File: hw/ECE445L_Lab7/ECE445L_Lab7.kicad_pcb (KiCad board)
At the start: 2 copper layers, 152.4 x 127 mm, 214 parts, among them J1 2479774-1, J2 EK-TM4C123GXL, J4 AudioJack, Q1 MMBF170, Q10 MMBF170, Q11 MMBF170, Q12 MMBF170, Q13 MMBF170, Q14 MMBF170, Q15 MMBF170, Q16 MMBF170, Q17 MMBF170, Q18 MMBF170, Q2 MMBF170, Q3 MMBF170, Q4 MMBF170, Q5 MMBF170, Q6 MMBF170, Q7 MMBF170, Q8 MMBF170, Q9 MMBF170, SW1 SW_SPST, SW2 Pause, SW3 LCDMode, SW4 Flanger, SW5 Distortion, SW6 Reverb, SW7 Delay, SW8 Tempo, U1 LM2937ET-3.3_NOPB, U10 TLV5616, U11 OPA2350, U12 OPA2350, U13 OPA2350, U14 OPA2350, U15 TLV5616, U16 Adafruit ST7735R, U2 LM4041CILPR, U3 ESP32-D0WD-V3, U5 FT232R, U6 OPA2350, U7 OPA2350, U8 OPA2350, U9 OPA2350

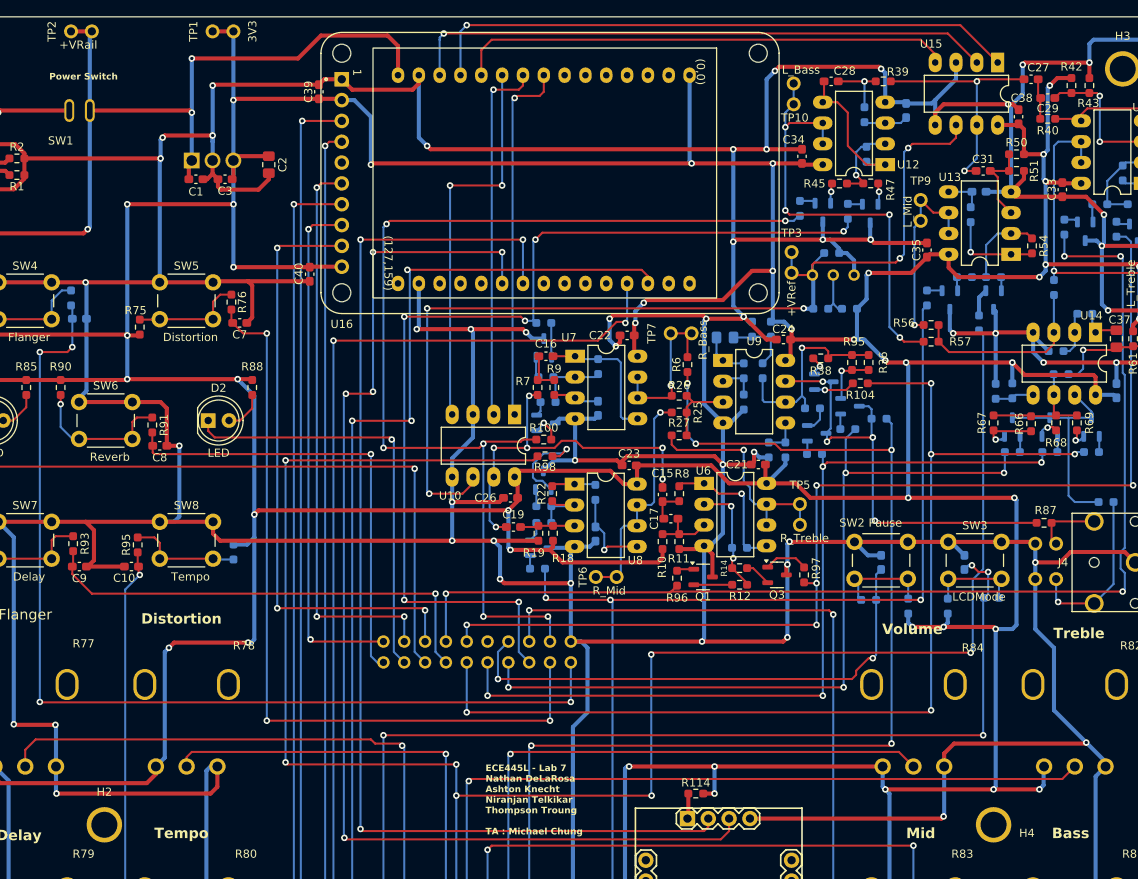
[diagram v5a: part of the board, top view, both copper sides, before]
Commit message: Hardware layout - fixed voltage reference
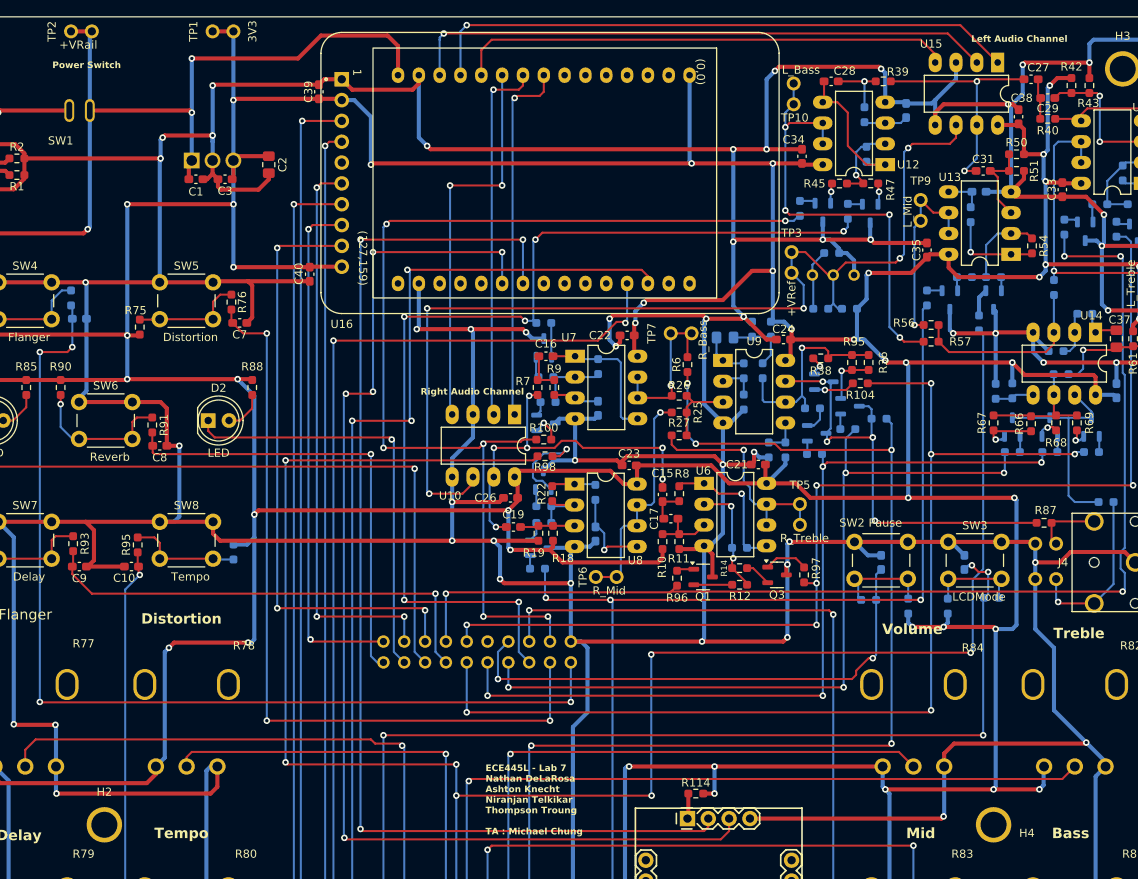
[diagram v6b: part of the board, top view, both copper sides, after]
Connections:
- R3 pad 2: Net-(R3-Pad2) -> VRef
- R4 pad 1: Net-(R3-Pad2) -> VRef
- R4 pad 2: VRef -> Net-(R4-Pad2)
- R5 pad 1: VRef -> Net-(R4-Pad2)
- U2 pad 1: VRef -> Net-(R4-Pad2)
- U2 pad 2: Net-(R3-Pad2) -> VRef
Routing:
- net Net-(R4-Pad2): track 0.00 -> 7.44 mm
- net Net-(R3-Pad2): track 5.69 -> 0.00 mm
- net VRef: track 122.0 -> 124.7 mm
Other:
- board text added: "Left Audio Channel"
- board text added: "Right Audio Channel"
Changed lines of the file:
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@@
 	(net 133 "Net-(C28-Pad2)")
 	(net 134 "Net-(C37-Pad2)")
-	(net 135 "Net-(R3-Pad2)")
+	(net 135 "Net-(R4-Pad2)")
 	(net 136 "Net-(Q7-B)")
 	(net 137 "unconnected-(U3-GPIO33-Pad7)")
@@
 		(at 101.6 44.45 -90)
 		(property "Reference" "U16"
-			(at 18.4404 25.4 180)
+			(at 18.4404 25.4 0)
 			(layer "F.SilkS")
 			(effects
@@
 		)
 		(fp_text user "(127,159)"
-			(at 7.62 20.32 270)
+			(at 7.0104 23.4188 270)
 			(unlocked yes)
 			(layer "F.SilkS")
@@
 			)
 		)
-		(pad "" np_thru_hole circle
-			(at -14.605 -25.4)
-			(size 2.2 2.2)
-			(drill 2.2)
-			(layers "*.Cu" "*.Mask")
-		)
-		(pad "" np_thru_hole circle
-			(at -14.605 25.4)
-			(size 2.2 2.2)
-			(drill 2.2)
-			(layers "*.Cu" "*.Mask")
-		)
-		(pad "" np_thru_hole circle
-			(at 14.605 -25.4)
-			(size 2.2 2.2)
-			(drill 2.2)
-			(layers "*.Cu" "*.Mask")
-		)
-		(pad "" np_thru_hole circle
-			(at 14.605 25.4)
-			(size 2.2 2.2)
-			(drill 2.2)
-			(layers "*.Cu" "*.Mask")
-		)
 		(pad "1" thru_hole rect
 			(at -11.43 25.4)
@@
 		)
 		(fp_line
-			(start -14.611 6.532)
-			(end -13.976 5.897)
-			(stroke
-				(width 0.2032)
-				(type solid)
-			)
-			(layer "F.SilkS")
-		)
-		(fp_line
-			(start -16.516 5.897)
-			(end -15.881 6.532)
-			(stroke
-				(width 0.2032)
-				(type solid)
-			)
-			(layer "F.SilkS")
-		)
-		(fp_line
 			(start -16.516 5.897)
 			(end -16.516 4.627)
@@
 		)
 		(fp_line
-			(start -16.516 4.627)
-			(end -15.881 3.992)
-			(stroke
-				(width 0.2032)
-				(type solid)
-			)
-			(layer "F.SilkS")
-		)
-		(fp_line
 			(start -13.976 4.627)
 			(end -13.976 5.897)
@@
 		)
 		(fp_line
-			(start -14.611 3.992)
-			(end -13.976 4.627)
-			(stroke
-				(width 0.2032)
-				(type solid)
-			)
-			(layer "F.SilkS")
-		)
-		(fp_line
 			(start -16.516 3.357)
 			(end -16.516 2.087)
@@
 			(layers "B.Cu" "B.Mask" "B.Paste")
 			(roundrect_rratio 0.25)
-			(net 135 "Net-(R3-Pad2)")
+			(net 100 "VRef")
 			(pintype "passive")
 		)
@@
 		)
 		(group ""
-			(members "11c5cd52-69f3-4446-bccb-5f9518d66313" "30eab901-faa1-48e6-9f11-a2470f24fe87"
-				"370ae8a8-94fd-461e-bf20-ddbf13826b6e" "3973a864-3621-4e61-8c96-8c65e393ac25"
-				"49d39620-b9be-450e-880b-1048b977e30c" "5eb9c70e-c6af-42c4-9062-bd827725a32c"
-				"678d534d-a7ca-4aa0-9f1e-a9d111543dec" "7488b676-18a6-4ed4-92f7-680afbb5b136"
-				"8022baee-523a-44e4-9ba1-32b8b3af9ea7" "9fb0d361-2e3e-429f-9451-9d610e9aa400"
-				"b61cd692-3c2b-4db4-a00d-1b86db24f691" "be1a233e-ac1f-4e60-93fe-5c93686e9edc"
-				"dd1363e2-d05e-4584-94b3-d17287d31c97" "ddfc8a73-91ee-4b8f-9319-b5ca49929a30"
-				"ee488e86-51e9-44a6-80ee-4de8811c40bf"
-			)
-		)
-		(group ""
 			(members "05085929-df47-4023-ada3-8e05809de806" "0d1c2b11-0e75-4697-914f-baecb480edc5"
 				"0d325539-8a40-476c-8c19-a88dd3c161f2" "1d2eddcb-aa38-4ea7-9334-7ec7fefdf58d"
@@
 			)
 		)
+		(group ""
+			(members "11c5cd52-69f3-4446-bccb-5f9518d66313" "30eab901-faa1-48e6-9f11-a2470f24fe87"
+				"370ae8a8-94fd-461e-bf20-ddbf13826b6e" "3973a864-3621-4e61-8c96-8c65e393ac25"
+				"49d39620-b9be-450e-880b-1048b977e30c" "5eb9c70e-c6af-42c4-9062-bd827725a32c"
+				"678d534d-a7ca-4aa0-9f1e-a9d111543dec" "7488b676-18a6-4ed4-92f7-680afbb5b136"
+				"8022baee-523a-44e4-9ba1-32b8b3af9ea7" "9fb0d361-2e3e-429f-9451-9d610e9aa400"
+				"b61cd692-3c2b-4db4-a00d-1b86db24f691" "be1a233e-ac1f-4e60-93fe-5c93686e9edc"
+				"dd1363e2-d05e-4584-94b3-d17287d31c97" "ddfc8a73-91ee-4b8f-9319-b5ca49929a30"
+				"ee488e86-51e9-44a6-80ee-4de8811c40bf"
+			)
+		)
 		(embedded_fonts no)
 		(model "${KICAD_USER_3DMODELS}/ESP32-30pin.step"
@@
 		(tags "SOT TO_SOT_SMD")
 		(property "Reference" "Q12"
-			(at 0 -2.4892 -90)
+			(at 0 -2.4892 270)
 			(layer "B.SilkS")
 			(effects
@@
 		(sheetname "/Lab7_microcontroller/")
 		(sheetfile "Lab7_microcontroller.kicad_sch")
-		(attr through_hole)
+		(attr through_hole allow_missing_courtyard)
 		(fp_line
 			(start 25.4 -33.02)
@@
 			(layers "B.Cu" "B.Mask" "B.Paste")
 			(roundrect_rratio 0.25)
-			(net 135 "Net-(R3-Pad2)")
+			(net 100 "VRef")
 			(pintype "passive")
 		)
@@
 			(layers "B.Cu" "B.Mask" "B.Paste")
 			(roundrect_rratio 0.25)
-			(net 100 "VRef")
+			(net 135 "Net-(R4-Pad2)")
 			(pintype "passive")
 		)
@@
 			(layers "B.Cu" "B.Mask" "B.Paste")
 			(roundrect_rratio 0.25)
-			(net 100 "VRef")
+			(net 135 "Net-(R4-Pad2)")
 			(pintype "passive")
 		)
@@
 			(layers "*.Cu" "*.Mask")
 			(remove_unused_layers no)
-			(net 100 "VRef")
+			(net 135 "Net-(R4-Pad2)")
 			(pintype "passive")
 			(solder_mask_margin 0.102)
@@
 			(layers "*.Cu" "*.Mask")
 			(remove_unused_layers no)
-			(net 135 "Net-(R3-Pad2)")
+			(net 100 "VRef")
 			(pintype "passive")
 			(solder_mask_margin 0.102)
@@
 		)
 	)
+	(gr_text "Right Audio Channel"
+		(at 85.8012 71.5772 0)
+		(layer "F.SilkS")
+		(effects
+			(font
+				(size 0.8 0.8)
+				(thickness 0.15)
+				(bold yes)
+			)
+			(justify left bottom)
+		)
+	)
 	(gr_text "Flanger"
 		(at 37.592 99.06 0)
@@
 		)
 	)
+	(gr_text "Left Audio Channel"
+		(at 152.9588 28.5496 0)
+		(layer "F.SilkS")
+		(effects
+			(font
+				(size 0.8 0.8)
+				(thickness 0.15)
+				(bold yes)
+			)
+			(justify left bottom)
+		)
+	)
 	(gr_text "Volume"
 		(at 145.796 100.838 0)
@@
 	)
 	(gr_text "Power Switch"
-		(at 40.513 33.147 0)
+		(at 40.894 31.75 0)
 		(layer "F.SilkS")
 		(effects
@@
 	)
 	(segment
-		(start 133.858 55.372)
-		(end 133.604 55.626)
+		(start 136.144 56.896)
+		(end 135.5344 56.896)
 		(width 0.25)
 		(layer "F.Cu")
@@
 	)
 	(segment
+		(start 136.144 56.896)
+		(end 137.668 55.372)
+		(width 0.25)
+		(layer "F.Cu")
+		(net 100)
+	)
+	(segment
+		(start 135.5344 56.896)
+		(end 132.7354 54.097)
+		(width 0.25)
+		(layer "F.Cu")
+		(net 100)
+	)
+	(segment
 		(start 86.868 83.566)
 		(end 90.932 83.566)
@@
 	)
 	(segment
-		(start 133.604 56.896)
-		(end 131.323 56.896)
+		(start 137.668 55.372)
+		(end 143.764 55.372)
 		(width 0.25)
 		(layer "F.Cu")
@@
 	)
 	(segment
-		(start 143.764 55.372)
-		(end 133.858 55.372)
+		(start 132.7354 54.097)
+		(end 131.064 54.097)
 		(width 0.25)
 		(layer "F.Cu")
@@
 	)
 	(segment
-		(start 133.604 55.626)
-		(end 133.604 56.896)
-		(width 0.25)
-		(layer "F.Cu")
-		(net 100)
-	)
-	(segment
 		(start 86.614 60.96)
 		(end 132.5372 60.96)
@@
 	)
 	(segment
+		(start 131.064 56.637)
+		(end 132.5372 58.1102)
+		(width 0.25)
+		(layer "B.Cu")
+		(net 100)
+	)
+	(segment
 		(start 144.272 54.864)
 		(end 144.78 54.356)
@@
 	)
 	(segment
-		(start 131.064 56.637)
-		(end 131.064 54.097)
+		(start 136.144 56.896)
+		(end 136.144 60.3993)
 		(width 0.25)
 		(layer "B.Cu")
@@
 	)
 	(segment
-		(start 133.7075 61.0108)
-		(end 132.588 61.0108)
-		(width 0.5)
+		(start 136.144 60.3993)
+		(end 135.5325 61.0108)
+		(width 0.25)
 		(layer "B.Cu")
 		(net 100)
 	)
 	(segment
-		(start 133.604 55.646403)
-		(end 135.0405 54.209903)
+		(start 131.064 56.637)
+		(end 131.064 54.097)
 		(width 0.25)
 		(layer "B.Cu")
@@
 	)
 	(segment
-		(start 133.604 56.896)
-		(end 133.604 55.646403)
+		(start 137.2127 61.0108)
+		(end 136.7555 61.0108)
 		(width 0.25)
 		(layer "B.Cu")
@@
 	)
 	(segment
-		(start 133.7075 56.9995)
-		(end 133.604 56.896)
-		(width 0.5)
+		(start 132.5372 58.1102)
+		(end 132.5372 60.96)
+		(width 0.25)
 		(layer "B.Cu")
 		(net 100)
 	)
 	(segment
-		(start 133.7075 61.0108)
-		(end 133.7075 56.9995)
-		(width 0.5)
+		(start 136.7555 61.0108)
+		(end 136.144 60.3993)
+		(width 0.25)
 		(layer "B.Cu")
 		(net 100)
@@
 	)
 	(segment
-		(start 136.144 56.896)
-		(end 136.144 60.3993)
+		(start 133.7075 61.0108)
+		(end 133.7075 56.9995)
 		(width 0.25)
 		(layer "B.Cu")
@@
 	)
 	(segment
-		(start 136.144 60.3993)
-		(end 135.5325 61.0108)
+		(start 133.604 55.646403)
+		(end 135.0405 54.209903)
 		(width 0.25)
 		(layer "B.Cu")
@@
 	)
 	(segment
-		(start 137.2127 61.0108)
-		(end 136.7555 61.0108)
+		(start 133.7075 56.9995)
+		(end 133.604 56.896)
 		(width 0.25)
 		(layer "B.Cu")
@@
 	)
 	(segment
-		(start 136.7555 61.0108)
-		(end 136.144 60.3993)
+		(start 133.604 56.896)
+		(end 133.604 55.646403)
 		(width 0.25)
 		(layer "B.Cu")

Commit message: Pushing so i can work on my desktop
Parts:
- added TP11: R_Out, ECE445L:Testpoint_1x02_P2.54mm, F.Cu at (175.2, 79.6)
- added TP12: L_Out, ECE445L:Testpoint_1x02_P2.54mm, F.Cu at (175.3, 71.8)
- moved C39 0.61 mm to (72.8, 34.6)
- moved U5 0.28 mm to (123.4, 138.2)
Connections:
- U3 pad 1: +3V3 -> +VRail
- U3 pad 10: RAUDIO_FS -> unconnected-(U3-GPIO32-Pad10)
- U3 pad 11: LAUDIO_FS -> unconnected-(U3-GPIO35-Pad11)
- U3 pad 12: LAUDIO_OUT -> unconnected-(U3-GPIO34-Pad12)
- U3 pad 13: LAUDIO_CLK -> unconnected-(U3-GPIO39-Pad13)
- U3 pad 14: GND -> unconnected-(U3-GPIO36-Pad14)
- U3 pad 15: +VRail -> +3V3
- U3 pad 17: unconnected-(U3-GPIO22-Pad17) -> GND
- U3 pad 18: PB0 -> unconnected-(U3-GPIO15-Pad18)
- U3 pad 19: PB1 -> unconnected-(U3-GPIO2-Pad19)
- U3 pad 2: unconnected-(U3-GPIO36-Pad2) -> GND
- U3 pad 21: unconnected-(U3-GPIO19-Pad21) -> ESP_OUT_USB_IN
- U3 pad 22: unconnected-(U3-GPIO18-Pad22) -> ESP_IN_USB_OUT
- U3 pad 24: ESP_IN_USB_OUT -> unconnected-(U3-GPIO18-Pad24)
- U3 pad 25: ESP_OUT_USB_IN -> unconnected-(U3-GPIO19-Pad25)
- U3 pad 27: unconnected-(U3-GPIO2-Pad27) -> PB1
- U3 pad 28: unconnected-(U3-GPIO15-Pad28) -> PB0
- U3 pad 29: GND -> unconnected-(U3-GPIO22-Pad29)
- U3 pad 3: unconnected-(U3-GPIO39-Pad3) -> LAUDIO_CLK
- U3 pad 4: unconnected-(U3-GPIO34-Pad4) -> LAUDIO_OUT
- U3 pad 5: unconnected-(U3-GPIO35-Pad5) -> LAUDIO_FS
- U3 pad 6: unconnected-(U3-GPIO32-Pad6) -> RAUDIO_FS
- U3 pad 7: unconnected-(U3-GPIO33-Pad7) -> RAUDIO_CLK
- U3 pad 9: RAUDIO_CLK -> unconnected-(U3-GPIO33-Pad9)
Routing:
- net GND: track 1171.8 -> 1129.7 mm, vias 54 -> 53
- net +VRail: track 271.3 -> 303.9 mm
- net PB0: track 150.1 -> 121.2 mm, vias 5 -> 4
- net LAUDIO_CLK: track 71.8 -> 46.2 mm
- net R_AudioOut: track 54.4 -> 77.1 mm, vias 4 -> 6
- net +3V3: track 910.0 -> 889.6 mm, vias 48 -> 45
- net LAUDIO_OUT: track 73.1 -> 52.9 mm
- net PB1: track 144.4 -> 125.3 mm
- net LAUDIO_FS: track 59.7 -> 44.7 mm, vias 0 -> 1
- net L_AudioOut: track 26.8 -> 37.2 mm, vias 0 -> 1
- net RAUDIO_FS: track 47.5 -> 57.5 mm
- net ESP_OUT_USB_IN: track 143.2 -> 152.4 mm
- net RAUDIO_CLK: track 44.5 -> 49.7 mm, vias 1 -> 2
- net ESP_IN_USB_OUT: track 140.8 -> 144.7 mm
- net Net-(U5A-3V3): track 2.95 -> 0.00 mm
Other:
- board text added: "Flanger Delay"
- board text added: "Flanger Frequency"
- board text removed: "Distortion"
- board text removed: "Flanger"

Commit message: Final PCB commit
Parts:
- removed the Q7 at (138.2, 72.9)
- removed the Q8 at (134.1, 76.2)
- removed the Q9 at (135.0, 69.9)
- removed R112, R113: 2k, Resistor_SMD:R_0603_1608Metric_Pad0.98x0.95mm_HandSolder
- removed the R32 at (130.3, 78.2)
- removed the R34 at (128.3, 78.2)
- removed the R35 at (138.4, 67.6)
- removed the R36 at (140.5, 67.6)
- removed the R37 at (133.6, 73.2)
- removed the R38 at (134.6, 67.1)
- removed the R63 at (158.0, 71.0)
- removed the R65 at (156.0, 71.1)
- removed the R66 at (160.3, 75.0)
- removed the R67 at (155.7, 74.9)
- removed the R68 at (163.3, 74.9)
- removed the R69 at (165.9, 74.9)
- removed the U5 at (123.4, 138.2)
- added D5: POWER, ECE445L:LED_D5.0mm, F.Cu at (57.1, 52.3)
- added G1: LOGO, LOGO, B.Cu at (122.0, 108.7)
- added Q13: MMBF170, Package_TO_SOT_SMD:SOT-23, F.Cu at (159.8, 80.0)
- added Q14: MMBF170, Package_TO_SOT_SMD:SOT-23, F.Cu at (160.0, 75.2)
- added Q15: MMBF170, Package_TO_SOT_SMD:SOT-23, F.Cu at (170.2, 76.7)
- added R100: 125, Resistor_SMD:R_0603_1608Metric_Pad0.98x0.95mm_HandSolder, B.Cu at (167.4, 74.9)
- added R101: 100, Resistor_SMD:R_0603_1608Metric_Pad0.98x0.95mm_HandSolder, B.Cu at (164.8, 73.9)
- added R105: 2k, Resistor_SMD:R_0603_1608Metric_Pad0.98x0.95mm_HandSolder, F.Cu at (166.9, 78.5)
- added R106: 125, Resistor_SMD:R_0603_1608Metric_Pad0.98x0.95mm_HandSolder, F.Cu at (133.9, 71.1)
- added R107: 100, Resistor_SMD:R_0603_1608Metric_Pad0.98x0.95mm_HandSolder, F.Cu at (133.9, 72.9)
- added R108: 75, Resistor_SMD:R_0603_1608Metric_Pad0.98x0.95mm_HandSolder, F.Cu at (133.9, 69.3)
- added R109: 2k, Resistor_SMD:R_0603_1608Metric_Pad0.98x0.95mm_HandSolder, B.Cu at (133.1, 73.7)
- added R110: 2k, Resistor_SMD:R_0603_1608Metric_Pad0.98x0.95mm_HandSolder, B.Cu at (137.7, 73.9)
- added R99: 1.5V, Resistor_SMD:R_0603_1608Metric_Pad0.98x0.95mm_HandSolder, F.Cu at (63.0, 51.3)
- added TP1: +3V3, ECE445L:Testpoint_1x02_P2.54mm, F.Cu at (142.2, 149.1)
- added TP4: GND, ECE445L:Testpoint_1x02_P2.54mm, F.Cu at (166.6, 149.1)
- added U4: FT232R, ECE445L:FT232R-Breakout, F.Cu at (123.4, 138.2)
- D1: value LED -> PD6
- D2: value LED -> PD7
- J3: renamed from J4; footprint ECE445L:Jack_3.5mm_CUI_SJ1-3523N_Horizontal -> ECE445L:STX3000
- Q1, Q16, Q17, Q18, Q2, Q3, Q4, Q5, Q6: footprint Package_TO_SOT_SMD:SOT-23-3 -> Package_TO_SOT_SMD:SOT-23
- Q10: renamed from Q13; footprint Package_TO_SOT_SMD:SOT-23-3 -> Package_TO_SOT_SMD:SOT-23
- Q11: renamed from Q14; footprint Package_TO_SOT_SMD:SOT-23-3 -> Package_TO_SOT_SMD:SOT-23
- Q12: renamed from Q15; footprint Package_TO_SOT_SMD:SOT-23-3 -> Package_TO_SOT_SMD:SOT-23
- Q7: renamed from Q10; footprint Package_TO_SOT_SMD:SOT-23-3 -> Package_TO_SOT_SMD:SOT-23
- Q8: renamed from Q11; footprint Package_TO_SOT_SMD:SOT-23-3 -> Package_TO_SOT_SMD:SOT-23
- Q9: renamed from Q12; footprint Package_TO_SOT_SMD:SOT-23-3 -> Package_TO_SOT_SMD:SOT-23
- R102: value 2k -> 75
- R103: moved to F.Cu
- R14: renamed from R10; value 100k -> 184k
- R15: renamed from R11; value 100k -> 68.8k
- R16: renamed from R12; value 20k -> 40k
- R17: renamed from R13; value 20k -> 40k
- R18: renamed from R14; value 10k -> 30k
- R19: renamed from R15; value 10k -> 30k
- R25: renamed from R18; value 100k -> 184k
- R26: renamed from R19; value 100k -> 68.8k
- R28: renamed from R20; value 20k -> 40k
- R30: renamed from R21; value 10k -> 30k
- R41: renamed from R33; value 100k -> 50k
- R47: renamed from R42; value 100k -> 184k
- R48: renamed from R43; value 100k -> 68.8k
- R49: renamed from R44; value 20k -> 40k
- R50: renamed from R45; value 20k -> 40k
- R51: renamed from R46; value 10k -> 30k
- R52: renamed from R47; value 10k -> 30k
- R58: renamed from R50; value 100k -> 184k
- R59: renamed from R51; value 100k -> 68.8k
- R60: renamed from R52; value 20k -> 40k
- R61: renamed from R53; value 10k -> 30k
- R72: renamed from R64; value 100k -> 50k
- TP2: renamed from TP1; value 3V3 -> +3V3
- moved Q18 29.5 mm to (138.9, 68.8), turned to 0 degrees
- moved R102 26.9 mm to (164.8, 75.7), turned to 0 degrees
- moved Q16 25.2 mm to (134.4, 66.8), turned to 0 degrees
- moved R111 23.4 mm to (135.1, 73.7), turned to 90 degrees
- moved R103 22.2 mm to (156.0, 80.8), turned to 0 degrees
- moved Q17 19.8 mm to (143.3, 70.9), turned to 0 degrees
- moved R104 17.8 mm to (156.2, 76.2), turned to 0 degrees
- moved R41 2.60 mm to (128.0, 71.1)
- moved J3 1.94 mm to (171.5, 90.7), turned to 180 degrees
- moved R96 1.37 mm to (170.7, 84.1), turned to 0 degrees
- moved R72 1.17 mm to (165.1, 69.0)
- moved D3 0.76 mm to (162.6, 89.7)
- moved D4 0.76 mm to (162.6, 94.0)
- moved TP7 0.51 mm to (131.6, 84.8)
- moved R11 0.51 mm to (116.6, 93.9)
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- renumbered C21 to C10, C22 to C11, C23 to C12, C24 to C13, C25 to C14, C26 to C15, C27 to C16, C28 to C17, C29 to C18, C30 to C19, C31 to C20, C32 to C21, C33 to C22, C34 to C23, C35 to C24, C36 to C25, C37 to C26, C38 to C27, C4 to C28, C5 to C29, C6 to C30, C7 to C31, C8 to C32, C9 to C33, C10 to C34, C39 to C35, C40 to C36, C15 to C4, C16 to C5, C17 to C6, C18 to C7, C19 to C8, C20 to C9, R8 to R10, R96 to R11, R9 to R12, R100 to R13, R16 to R20, R17 to R21, R97 to R22, R101 to R23, R98 to R24, R6 to R27, R23 to R29, R22 to R31, R99 to R32, R24 to R33, R25 to R34, R26 to R35, R27 to R36, R28 to R37, R29 to R38, R30 to R39, R31 to R40, R39 to R42, R40 to R43, R109 to R44, R107 to R45, R41 to R46, R48 to R53, R49 to R54, R110 to R55, R108 to R56, R105 to R57, R114 to R6, R54 to R62, R106 to R63, R55 to R64, R58 to R65, R56 to R66, R57 to R67, R59 to R68, R60 to R69, R115 to R7, R61 to R70, R62 to R71, R70 to R73, R89 to R74, R71 to R75, R72 to R76, R73 to R77, R74 to R78, R75 to R79, R116 to R8, R76 to R80, R90 to R81, R91 to R82, R77 to R83, R92 to R84, R93 to R85, R78 to R86, R79 to R87, R94 to R88, R95 to R89, R7 to R9, R80 to R90, R81 to R91, R82 to R92, R83 to R93, R84 to R94, R85 to R95, R86 to R96, R87 to R97, R88 to R98, TP8 to TP10, TP9 to TP11, TP10 to TP12, TP11 to TP13, TP12 to TP14, TP4 to TP3, TP2 to TP5, TP3 to TP6, TP5 to TP7, TP6 to TP8, TP7 to TP9, U11 to U10, U12 to U11, U13 to U12, U14 to U13, U15 to U14, U16 to U15, U6 to U5, U7 to U6, U8 to U7, U9 to U8, U10 to U9
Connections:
- C14 pad 2: Net-(C25-Pad2) -> Net-(U8B-+)
- C26 pad 2: Net-(C37-Pad2) -> Net-(U13B-+)
- Q1 pad 2: Net-(Q1-C) -> GND
- Q1 pad 3: GND -> Net-(Q1-D)
- Q10 pad 2: Net-(Q13-C) -> GND
- Q10 pad 3: GND -> Net-(Q10-D)
- Q11 pad 2: Net-(Q14-C) -> GND
- Q11 pad 3: GND -> Net-(Q11-D)
- Q12 pad 2: Net-(Q15-C) -> GND
- Q12 pad 3: GND -> Net-(Q12-D)
- Q16 pad 1: Net-(Q16-B) -> Net-(Q16-G)
- Q16 pad 2: Net-(Q16-C) -> R_AudioOut
- Q16 pad 3: L_AudioOut -> Net-(Q16-D)
- Q17 pad 2: Net-(Q17-C) -> R_AudioOut
- Q17 pad 3: L_AudioOut -> Net-(Q17-D)
- Q18 pad 1: Net-(Q18-B) -> Net-(Q18-G)
- Q18 pad 2: Net-(Q18-C) -> R_AudioOut
- Q18 pad 3: L_AudioOut -> Net-(Q18-D)
- Q2 pad 2: Net-(Q2-C) -> GND
- Q2 pad 3: GND -> Net-(Q2-D)
- Q3 pad 2: Net-(Q3-C) -> GND
- Q3 pad 3: GND -> Net-(Q3-D)
- Q4 pad 2: Net-(Q4-C) -> GND
- Q4 pad 3: GND -> Net-(Q4-D)
- Q5 pad 2: Net-(Q5-C) -> GND
- Q5 pad 3: GND -> Net-(Q5-D)
- Q6 pad 2: Net-(Q6-C) -> GND
- Q6 pad 3: GND -> Net-(Q6-D)
- Q7 pad 2: Net-(Q10-C) -> GND
- Q7 pad 3: GND -> Net-(Q7-D)
- Q8 pad 2: Net-(Q11-C) -> GND
- Q8 pad 3: GND -> Net-(Q8-D)
- Q9 pad 2: Net-(Q12-C) -> GND
- Q9 pad 3: GND -> Net-(Q9-D)
- R102 pad 1: PC4 -> Net-(Q13-D)
- R102 pad 2: Net-(Q7-B) -> L_AudioBuf
- R103 pad 1: PC5 -> PC4
- R104 pad 1: PC6 -> PC5
- R111 pad 1: Net-(Q16-B) -> PC6
- R111 pad 2: PC4 -> Net-(Q18-G)
- R16 pad 2: Net-(Q1-C) -> Net-(Q1-D)
- R17 pad 2: Net-(Q2-C) -> Net-(Q2-D)
- R18 pad 1: Net-(Q3-C) -> Net-(Q3-D)
- R19 pad 1: Net-(Q4-C) -> Net-(Q4-D)
- R28 pad 2: Net-(Q5-C) -> Net-(Q5-D)
- R30 pad 1: Net-(Q6-C) -> Net-(Q6-D)
- R39 pad 1: Net-(C25-Pad2) -> Net-(U8B-+)
- R40 pad 2: Net-(C25-Pad2) -> Net-(U8B-+)
- R41 pad 1: Net-(C25-Pad2) -> R_AudioBuf
- R49 pad 2: Net-(Q10-C) -> Net-(Q7-D)
- R50 pad 2: Net-(Q11-C) -> Net-(Q8-D)
- R51 pad 2: Net-(Q12-C) -> Net-(Q9-D)
- R52 pad 2: Net-(Q13-C) -> Net-(Q10-D)
- R60 pad 2: Net-(Q14-C) -> Net-(Q11-D)
- R61 pad 2: Net-(Q15-C) -> Net-(Q12-D)
- R70 pad 1: Net-(C37-Pad2) -> Net-(U13B-+)
- R71 pad 2: Net-(C37-Pad2) -> Net-(U13B-+)
- R72 pad 1: Net-(C37-Pad2) -> L_AudioBuf
- R96 pad 2: L_AudioOut -> R_AudioOut
- R97 pad 2: R_AudioOut -> L_AudioOut
- U13 pad 5: Net-(U14B-+) -> Net-(U13B-+)
- U13 pad 7: L_AudioOut -> L_AudioBuf
- U8 pad 5: Net-(U9B-+) -> Net-(U8B-+)
- U8 pad 7: R_AudioOut -> R_AudioBuf
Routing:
- net GND: track 1129.7 -> 1155.1 mm, vias 53 -> 55
- net Net-(U8B--): track 24.7 -> 2.44 mm, vias 1 -> 0
- net Net-(U8B-+): track 0.00 -> 18.3 mm
- net Net-(U13B-+): track 0.00 -> 17.0 mm, vias 0 -> 1
- net L_AudioOut: track 37.2 -> 52.6 mm, vias 1 -> 5
- net PB6: track 140.8 -> 125.9 mm, vias 4 -> 6
- net PC6: track 129.2 -> 115.6 mm, vias 5 -> 3
- net Net-(C37-Pad2): track 11.7 -> 0.00 mm, vias 1 -> 0
- net Net-(U13B--): track 14.7 -> 2.99 mm
- net Net-(Q17-D): track 0.00 -> 11.2 mm, vias 0 -> 1
- net R_AudioOut: track 77.1 -> 65.9 mm, vias 6 -> 2
- net R_AudioBuf: track 0.00 -> 8.84 mm
- net L_AudioBuf: track 0.00 -> 8.64 mm
- net Net-(C25-Pad2): track 8.11 -> 0.00 mm
- net Net-(Q18-D): track 0.00 -> 7.29 mm, vias 0 -> 1
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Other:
- board text added: "UTX_FALL_2025 NNAT Nathan DeLaRosa Ashton Knecht Niranjan Telkikar Thompson Troung ECE445L TA : Michael Chung"
- board text removed: "ECE445L - Lab 7 Nathan DeLaRosa Ashton Knecht Niranjan Telkikar Thompson Troung TA : Michael Chung"
